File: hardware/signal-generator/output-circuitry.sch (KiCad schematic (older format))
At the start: 40 parts, among them U15 MCP4651-502E/ST, U16 AZ431AN-A, U17 AD8021ARZ, U18 MCP4551-103E/MS, U19 AD8021ARZ, U20 AD8021ARZ, U21 AD8021ARZ

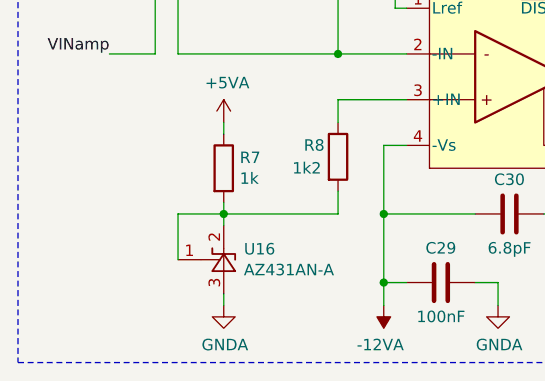
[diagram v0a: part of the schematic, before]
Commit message: [Signal Generator] Decouple voltage references with capacitors
Both the AZ431-A (+2.5V) and the TS4061 (+1.25V) voltage references have
been decoupled to GND with 100nF capacitors.
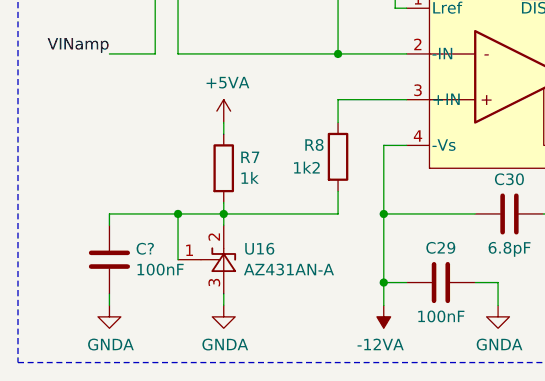
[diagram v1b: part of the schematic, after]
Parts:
- added C?: 100nF, symbol Device:C
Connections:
- net GNDA: now also C?.2
- net at R7.2, R8.2, U16.1 (REF)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: now also C?.1
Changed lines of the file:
@@
 Sheet 4 6
 Title "Digital Function Generator v2 - Output Circuitry"
-Date "2019-12-15"
+Date "2019-12-20"
 Rev "1"
 Comp "Petar Nikolov"
@@
 	1750 6550 1750 6600
 Wire Wire Line
-	1750 6600 2250 6600
-Wire Wire Line
 	7550 2300 7150 2300
 Connection ~ 7150 2300
@@
 Wire Wire Line
 	1350 3950 1550 3950
+Wire Wire Line
+	1550 6800 1550 6600
+Wire Wire Line
+	1550 6600 1750 6600
+Wire Wire Line
+	4450 2100 5150 2100
+Connection ~ 5150 2100
+Wire Wire Line
+	5150 2100 5250 2100
+Wire Wire Line
+	5150 2100 5150 2600
+Wire Wire Line
+	4450 2300 4650 2300
+Wire Wire Line
+	4650 2300 4650 2600
+Connection ~ 4650 2300
+Wire Wire Line
+	4650 2300 5250 2300
+Wire Wire Line
+	9000 5250 9400 5250
+Wire Wire Line
+	8900 5250 9000 5250
+Connection ~ 9000 5250
+Wire Wire Line
+	7850 5250 8600 5250
+Connection ~ 7850 5250
+Wire Notes Line
+	10800 3700 10800 6400
+Wire Notes Line
+	8350 3700 10800 3700
+Wire Notes Line
+	8350 6400 10800 6400
+$Comp
+L Device:C C?
+U 1 1 5E01B992
+P 1250 6800
+F 0 "C?" H 1365 6846 50  0000 L CNN
+F 1 "100nF" H 1365 6755 50  0000 L CNN
+F 2 "" H 1288 6650 50  0001 C CNN
+F 3 "~" H 1250 6800 50  0001 C CNN
+	1    1250 6800
+	1    0    0    -1
+$EndComp
+Wire Wire Line
+	1750 6600 2250 6600
 $Comp
 L ulib_Voltage_References:AZ431AN-A U16
@@
 $EndComp
 Wire Wire Line
-	1550 6800 1550 6600
-Wire Wire Line
-	1550 6600 1750 6600
-Wire Wire Line
-	4450 2100 5150 2100
-Connection ~ 5150 2100
-Wire Wire Line
-	5150 2100 5250 2100
-Wire Wire Line
-	5150 2100 5150 2600
-Wire Wire Line
-	4450 2300 4650 2300
-Wire Wire Line
-	4650 2300 4650 2600
-Connection ~ 4650 2300
-Wire Wire Line
-	4650 2300 5250 2300
-Wire Wire Line
-	9000 5250 9400 5250
-Wire Wire Line
-	8900 5250 9000 5250
-Connection ~ 9000 5250
-Wire Wire Line
-	7850 5250 8600 5250
-Connection ~ 7850 5250
-Wire Notes Line
-	10800 3700 10800 6400
-Wire Notes Line
-	8350 3700 10800 3700
-Wire Notes Line
-	8350 6400 10800 6400
+	1250 6950 1250 7000
+$Comp
+L power:GNDA #PWR?
+U 1 1 5E04C277
+P 1250 7000
+F 0 "#PWR?" H 1250 6750 50  0001 C CNN
+F 1 "GNDA" H 1255 6827 50  0000 C CNN
+F 2 "" H 1250 7000 50  0001 C CNN
+F 3 "" H 1250 7000 50  0001 C CNN
+	1    1250 7000
+	1    0    0    -1
+$EndComp
+Wire Wire Line
+	1250 6650 1250 6600
+Wire Wire Line
+	1250 6600 1550 6600
+Connection ~ 1550 6600
 $EndSCHEMATC

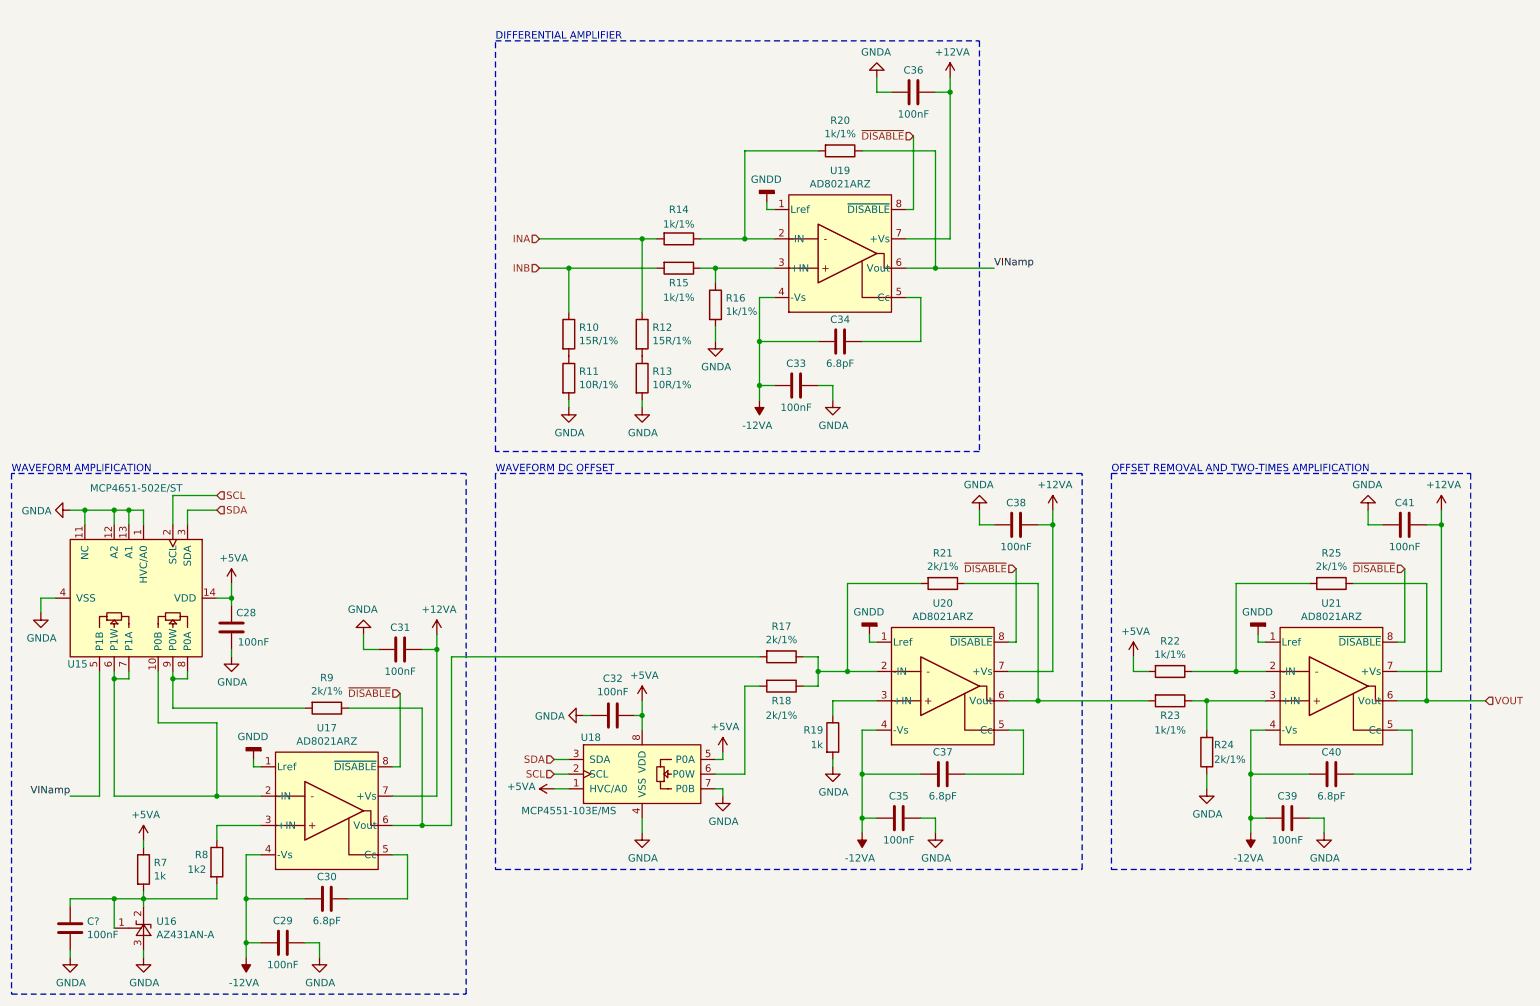
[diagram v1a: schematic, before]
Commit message: [Signal Generator] Change LCD backlight control method
The LCD's backlight was previously intended to be controlled via a
digital potentiometer. However, a much more elegant solution is to
control said backlight via PWM.

Also, removed the level shifter schematic sheet. The level shifters have been
moved to the TFT module's schematic sheet.
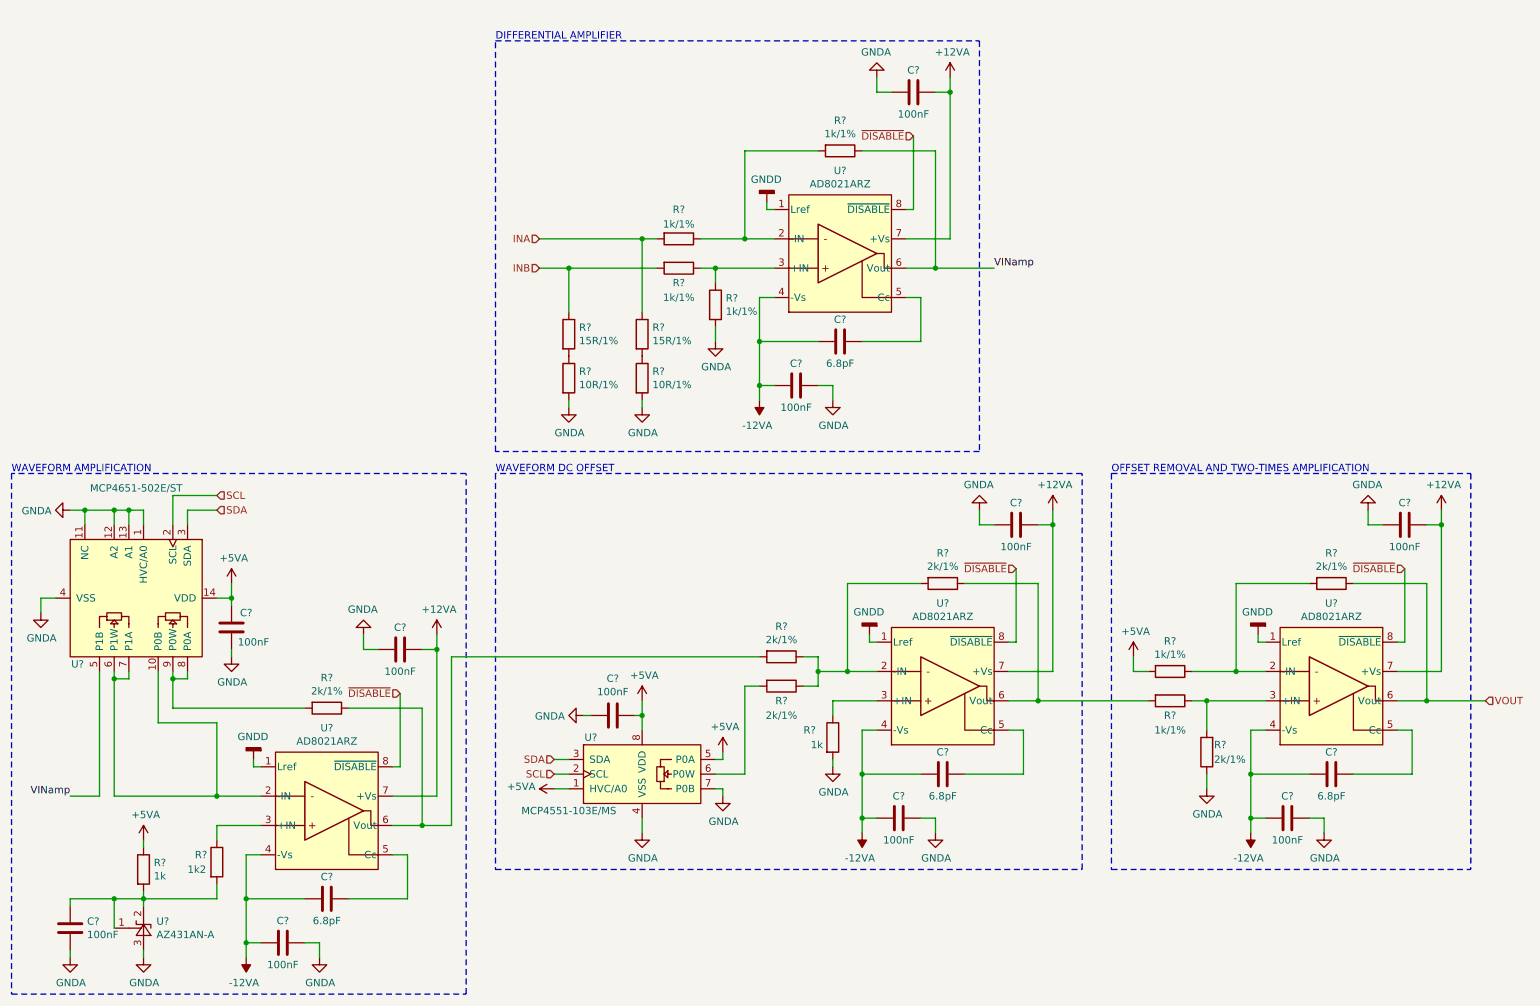
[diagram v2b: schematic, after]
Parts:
- renumbered C30 to C?, C29 to C?, C37 to C?, C35 to C?, C38 to C?, C28 to C?, C31 to C?, C40 to C?, C39 to C?, C41 to C?, C32 to C?, C34 to C?, C36 to C?, C33 to C?, R21 to R?, R19 to R?, R18 to R?, R17 to R?, R9 to R?, R25 to R?, R22 to R?, R24 to R?, R23 to R?, R20 to R?, R16 to R?, R8 to R?, R15 to R?, R14 to R?, R12 to R?, R10 to R?, R11 to R?, R13 to R?, R7 to R?, U17 to U?, U20 to U?, U15 to U?, U21 to U?, U18 to U?, U19 to U?, U16 to U?

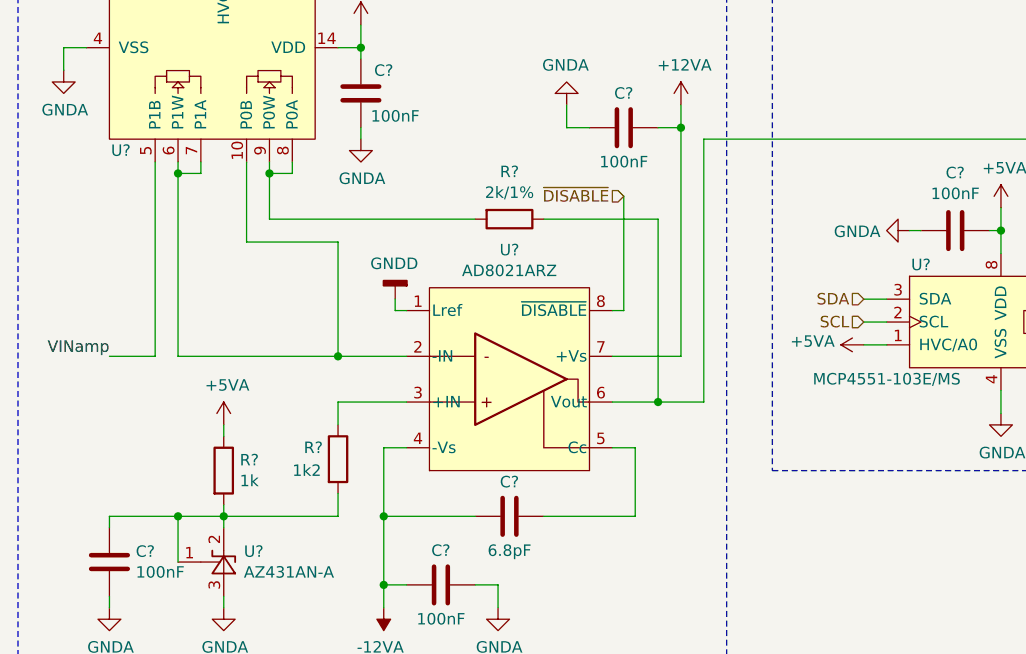
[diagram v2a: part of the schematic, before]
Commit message: [Signal Generator] Minor changes
1) Decouple AREF to GNDD with 100nF capacitor. The ATmega's internal ADC
will be used to calibrate the output circuitry's digital potentiometers.

2) Change I2C address of output DC offset digital potentiometer
(MCP4551) from '0101 111' to '0101 110'.
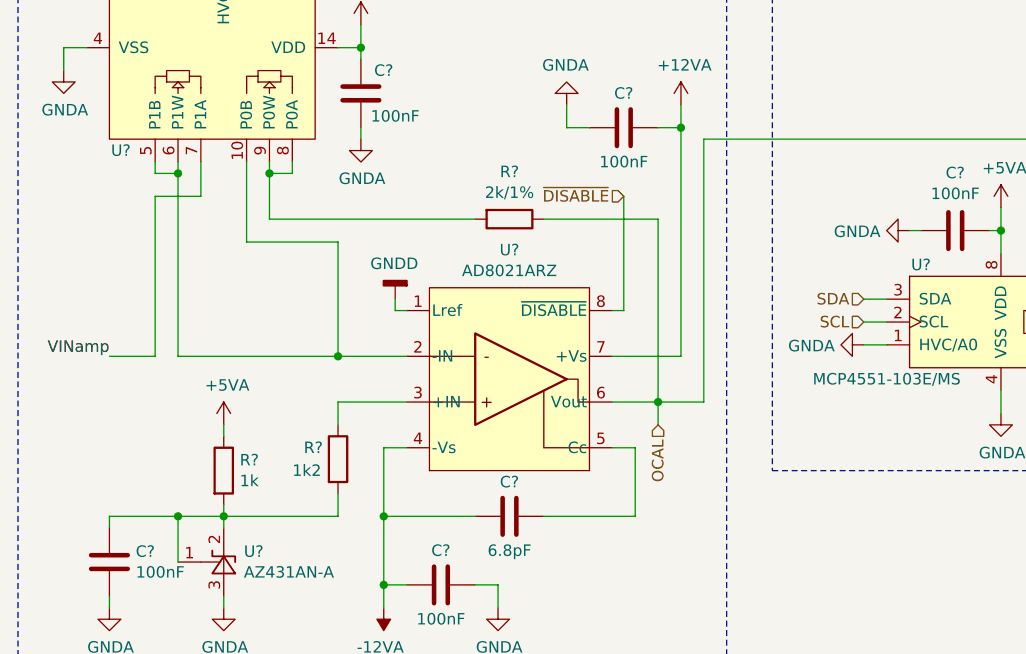
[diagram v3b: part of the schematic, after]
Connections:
- net +5VA: no longer U?.1 (HVC/A0)
- net GNDA: now also U?.1 (HVC/A0)
- net VINamp: now also U?.7 (P1A); no longer U?.5 (P1B)
- net at U?.10 (P0B), U?.2 (-IN), U?.6 (P1W): now also U?.5 (P1B); no longer U?.7 (P1A)
- net OCAL: now reaches R?.1, R?.2, U?.6 (Vout)
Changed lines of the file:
@@
 Sheet 4 5
 Title "Digital Function Generator v2 - Output Circuitry"
-Date "2019-12-20"
+Date "2019-12-21"
 Rev "1"
 Comp "Petar Nikolov"
@@
 Wire Wire Line
 	2050 5100 2050 5050
-Wire Wire Line
-	1650 5050 1650 5100
-Wire Wire Line
-	1650 5100 1550 5100
-Wire Wire Line
-	1550 5100 1550 5050
 Connection ~ 1950 5100
-Connection ~ 1550 5100
 Wire Wire Line
 	3450 6100 3650 6100
@@
 $Comp
 L power:+5VA #PWR?
-U 1 1 5DF1680B
-P 4550 5850
-F 0 "#PWR?" H 4550 5700 50  0001 C CNN
-F 1 "+5VA" V 4565 5977 50  0000 L CNN
-F 2 "" H 4550 5850 50  0001 C CNN
-F 3 "" H 4550 5850 50  0001 C CNN
-	1    4550 5850
-	0    -1   -1   0
-$EndComp
-$Comp
-L power:+5VA #PWR?
 U 1 1 5DF338CA
 P 5700 5600
@@
 	1850 5050 1850 5400
 Wire Wire Line
-	1550 5100 1550 5900
-Wire Wire Line
 	1550 5900 2250 5900
 Wire Wire Line
 	1450 5900 1250 5900
-Wire Wire Line
-	1450 5050 1450 5900
 Wire Wire Line
 	10900 5250 10500 5250
@@
 WAVEFORM DC OFFSET
 Wire Wire Line
-	3850 4950 5950 4950
-Wire Wire Line
 	3850 4950 3850 6100
 Wire Notes Line
@@
 	1250 6600 1550 6600
 Connection ~ 1550 6600
+Wire Wire Line
+	1550 5050 1550 5100
+Wire Wire Line
+	1450 5050 1450 5100
+Wire Wire Line
+	1450 5100 1550 5100
+Connection ~ 1550 5100
+Wire Wire Line
+	1550 5100 1550 5900
+Wire Wire Line
+	1650 5200 1450 5200
+Wire Wire Line
+	1450 5200 1450 5900
+Wire Wire Line
+	1650 5050 1650 5200
+$Comp
+L power:GNDA #PWR?
+U 1 1 5E095BC7
+P 4550 5850
+F 0 "#PWR?" H 4550 5600 50  0001 C CNN
+F 1 "GNDA" V 4555 5723 50  0000 R CNN
+F 2 "" H 4550 5850 50  0001 C CNN
+F 3 "" H 4550 5850 50  0001 C CNN
+	1    4550 5850
+	0    1    1    0
+$EndComp
+Wire Wire Line
+	3850 4950 5950 4950
+Wire Wire Line
+	3650 6100 3650 6200
+Text HLabel 3650 6200 3    50   Input ~ 0
+OCAL
 $EndSCHEMATC

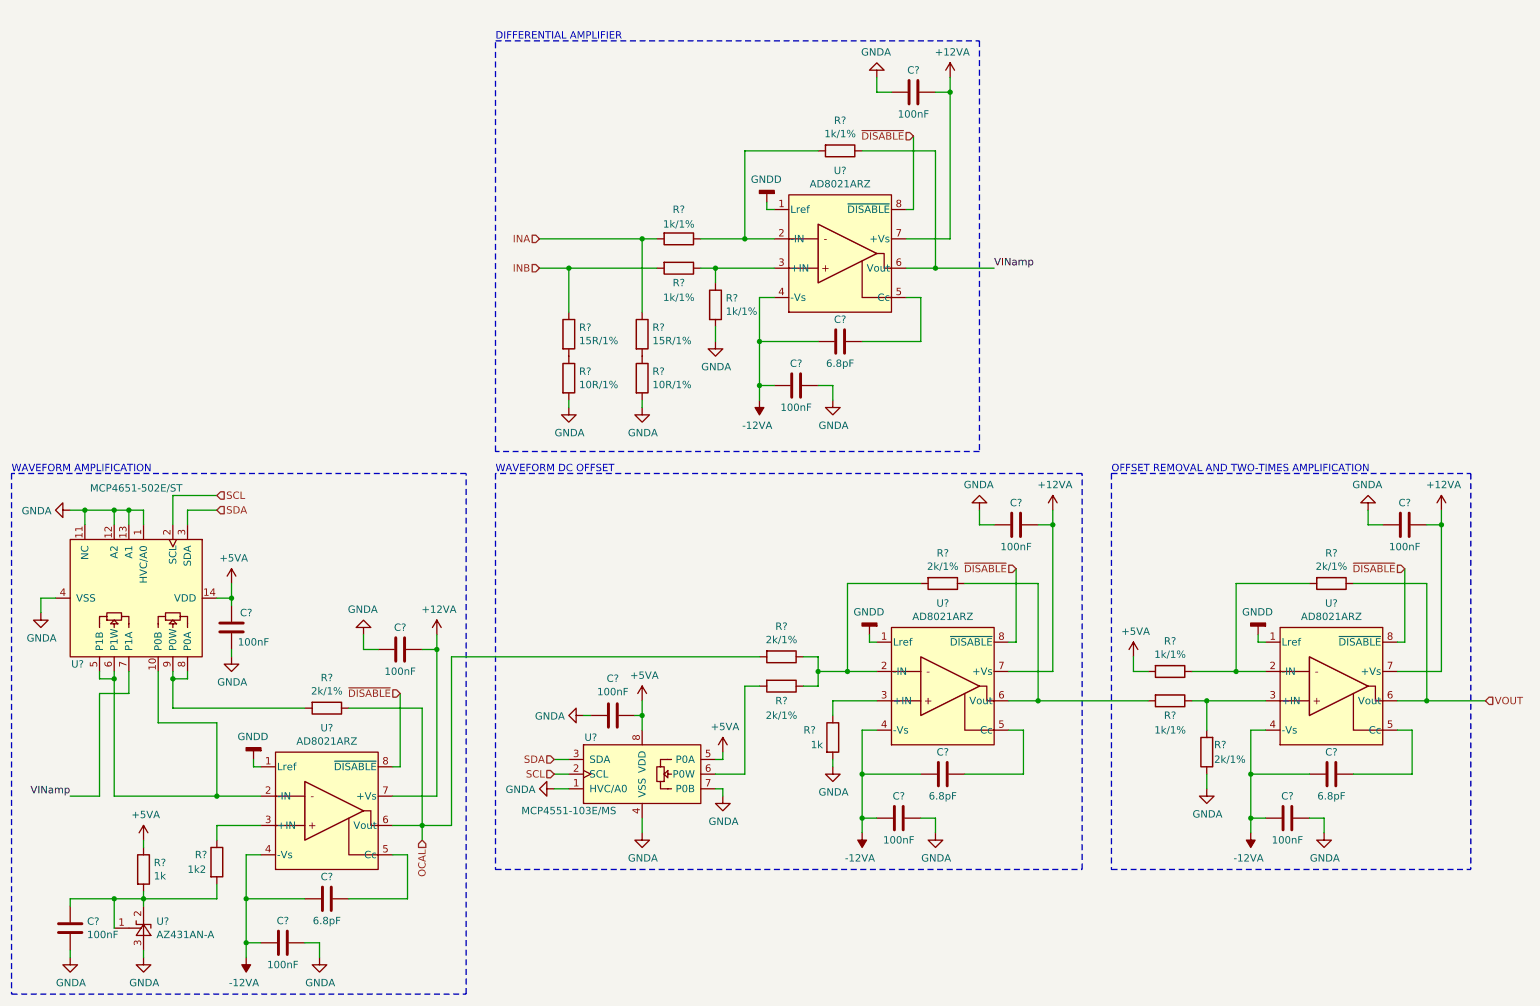
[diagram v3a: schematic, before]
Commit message: [Signal Generator] Finalize schematic
The electronic schematic is now finalized. All components have been
annotated. Furthermore, all components have an appropriate footprint
associated to them.
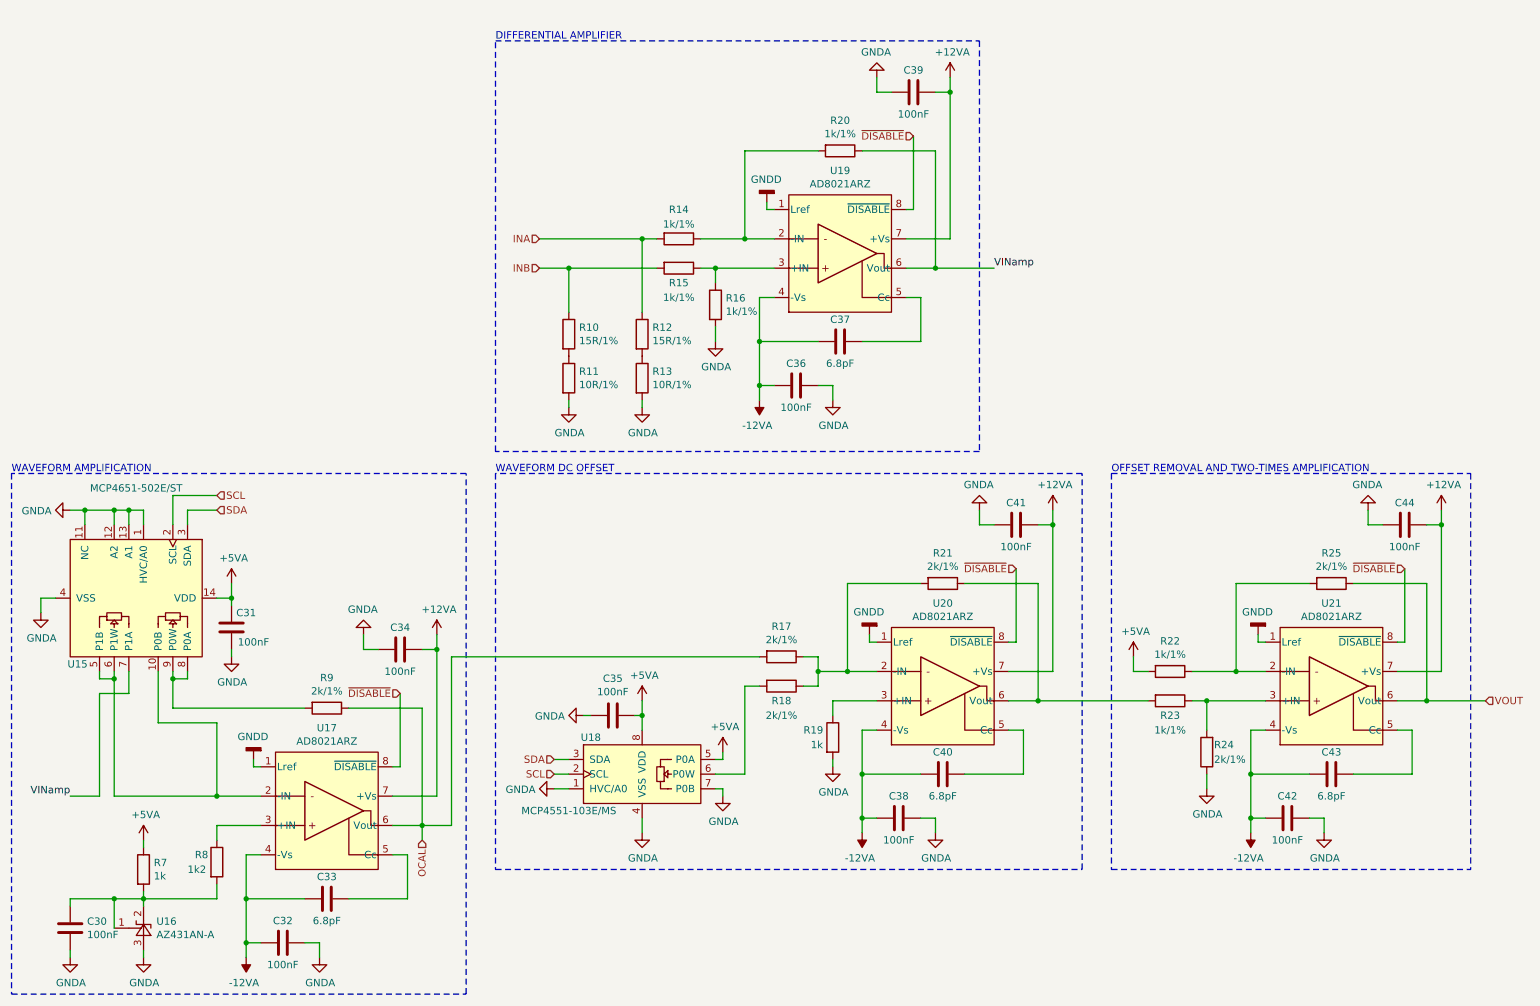
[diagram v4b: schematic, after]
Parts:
- C30: renamed from C?; footprint (none) -> Capacitors_SMD:C_0805_HandSoldering
- gave numbers to parts that had none: 40
